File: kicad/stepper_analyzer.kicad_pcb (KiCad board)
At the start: 2 copper layers, 102 x 57 mm, 23 parts, among them J1 Connector_Conn_01x04_Male, J2 Connector_Conn_01x04_Male, M1 Motor, Q1 AO3400A, U1 ACS70331EOLCTR-2P5B3, U2 ACS70331EOLCTR-2P5B3, U3 Pico

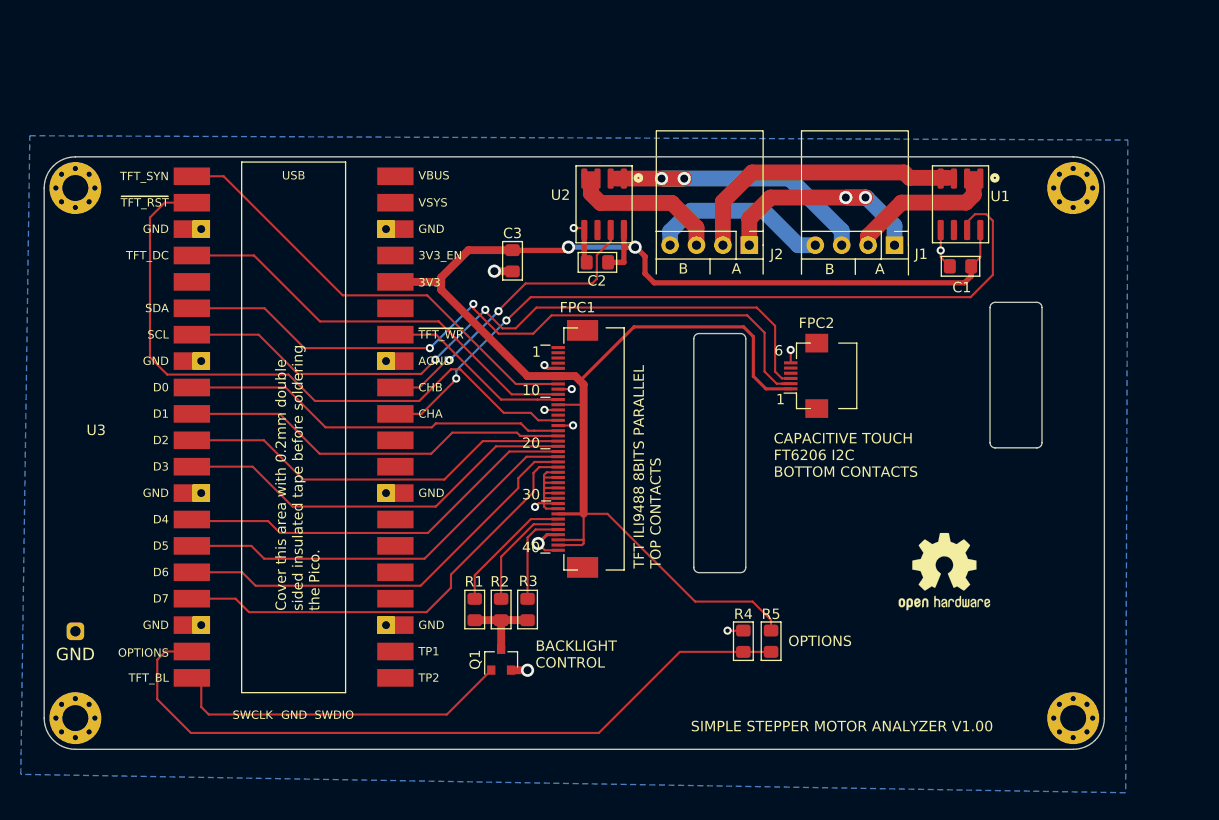
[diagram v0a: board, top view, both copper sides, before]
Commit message: First version, v1.0 of feather
2 stepper motor support using the ACS70311 sensors
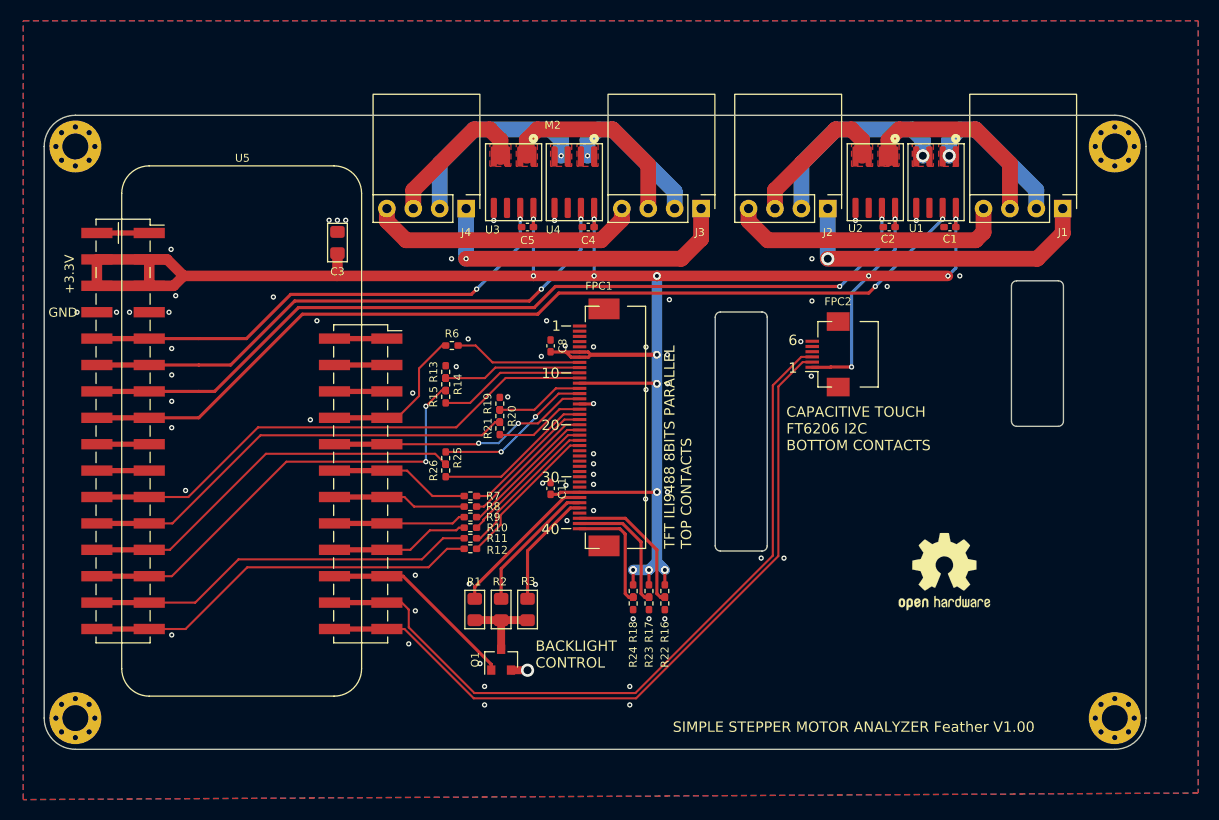
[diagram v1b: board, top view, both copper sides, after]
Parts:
- removed R4, R5: DNP, stepper_motor_analyzer:R_0805_2012Metric_Pad1.15x1.40mm_HandSolder_no_3d
- removed TP3: TestPoint, stepper_motor_analyzer:testpoint_double_side
- added C11: 1u, Capacitor_SMD:C_0402_1005Metric_Pad0.74x0.62mm_HandSolder, F.Cu at (47.7, -25.1)
- added C4: 0.1u, Capacitor_SMD:C_0402_1005Metric_Pad0.74x0.62mm_HandSolder, F.Cu at (51.3, -50.2)
- added C5: 0.1u, Capacitor_SMD:C_0402_1005Metric_Pad0.74x0.62mm_HandSolder, F.Cu at (45.5, -50.2)
- added C8: 1u, Capacitor_SMD:C_0402_1005Metric_Pad0.74x0.62mm_HandSolder, F.Cu at (47.7, -38.8)
- added J3: Connector_Conn_01x04_Male, stepper_motor_analyzer:connector_4pins_horizontal, F.Cu at (62.2, -52.0)
- added J4: Connector_Conn_01x04_Male, stepper_motor_analyzer:connector_4pins_horizontal, F.Cu at (39.6, -52.0)
- added M2: Motor, stepper_motor_analyzer:null_footprint, F.Cu at (36.4, -57.6)
- added R10: 0, Resistor_SMD:R_0402_1005Metric_Pad0.72x0.64mm_HandSolder, F.Cu at (40.0, -21.3)
- added R11: 0, Resistor_SMD:R_0402_1005Metric_Pad0.72x0.64mm_HandSolder, F.Cu at (40.0, -20.3)
- added R12: 0, Resistor_SMD:R_0402_1005Metric_Pad0.72x0.64mm_HandSolder, F.Cu at (40.0, -19.3)
- added R13: 0, Resistor_SMD:R_0402_1005Metric_Pad0.72x0.64mm_HandSolder, F.Cu at (37.6, -36.3)
- added R14: no_stuff, Resistor_SMD:R_0402_1005Metric_Pad0.72x0.64mm_HandSolder, F.Cu at (37.6, -35.1)
- added R15: 0, Resistor_SMD:R_0402_1005Metric_Pad0.72x0.64mm_HandSolder, F.Cu at (37.6, -33.9)
- added R16: 0, Resistor_SMD:R_0402_1005Metric_Pad0.72x0.64mm_HandSolder, F.Cu at (58.7, -15.2)
- added R17: 0, Resistor_SMD:R_0402_1005Metric_Pad0.72x0.64mm_HandSolder, F.Cu at (57.2, -15.2)
- added R18: no_stuff, Resistor_SMD:R_0402_1005Metric_Pad0.72x0.64mm_HandSolder, F.Cu at (55.7, -15.2)
- added R19: 0, Resistor_SMD:R_0402_1005Metric_Pad0.72x0.64mm_HandSolder, F.Cu at (42.8, -33.3)
- added R20: no_stuff, Resistor_SMD:R_0402_1005Metric_Pad0.72x0.64mm_HandSolder, F.Cu at (42.8, -32.1)
- added R21: 0, Resistor_SMD:R_0402_1005Metric_Pad0.72x0.64mm_HandSolder, F.Cu at (42.8, -30.9)
- added R22: no_stuff, Resistor_SMD:R_0402_1005Metric_Pad0.72x0.64mm_HandSolder, F.Cu at (58.7, -14.0)
- added R23: no_stuff, Resistor_SMD:R_0402_1005Metric_Pad0.72x0.64mm_HandSolder, F.Cu at (57.2, -14.0)
- added R24: 0, Resistor_SMD:R_0402_1005Metric_Pad0.72x0.64mm_HandSolder, F.Cu at (55.7, -14.0)
- added R25: no_stuff, Resistor_SMD:R_0402_1005Metric_Pad0.72x0.64mm_HandSolder, F.Cu at (37.6, -28.0)
- added R26: 0, Resistor_SMD:R_0402_1005Metric_Pad0.72x0.64mm_HandSolder, F.Cu at (37.6, -26.8)
- added R6: 0, Resistor_SMD:R_0402_1005Metric_Pad0.72x0.64mm_HandSolder, F.Cu at (38.2, -38.8)
- added R7: 0, Resistor_SMD:R_0402_1005Metric_Pad0.72x0.64mm_HandSolder, F.Cu at (40.0, -24.4)
- added R8: 0, Resistor_SMD:R_0402_1005Metric_Pad0.72x0.64mm_HandSolder, F.Cu at (40.0, -23.4)
- added R9: 0, Resistor_SMD:R_0402_1005Metric_Pad0.72x0.64mm_HandSolder, F.Cu at (40.0, -22.3)
- added U4: ACS70331EOLCTR-2P5B3, stepper_motor_analyzer:SOIC-8_3.9x4.9mm_P1.27mm, F.Cu at (50.0, -54.6)
- added U5: Adafruit_Feather_RP2040, stepper_motor_analyzer:Adafruit_Feather_SMD_2H, F.Cu at (18.0, -30.8)
- C1, C2: footprint stepper_motor_analyzer:C_0805_2012Metric_Pad1.15x1.40mm_HandSolder -> Capacitor_SMD:C_0402_1005Metric_Pad0.74x0.62mm_HandSolder
- U3: value Pico -> ACS70331EOLCTR-2P5B3; footprint stepper_motor_analyzer:Pico_smd_dedicated -> stepper_motor_analyzer:SOIC-8_3.9x4.9mm_P1.27mm
- moved U3 31.7 mm to (44.2, -54.6), turned to -90 degrees
- moved C2 28.3 mm to (80.3, -50.2)
- moved U2 26.2 mm to (79.0, -54.6)
- moved C3 16.9 mm to (27.2, -48.8), turned to -90 degrees
- moved J1 16.6 mm to (97.0, -52.0)
- moved J2 8.33 mm to (74.4, -52.0)
- moved H3 5.66 mm to (102.0, -58.0)
- moved H2 4.00 mm to (2.00, -58.0)
- moved H4 4.00 mm to (102.0, -3.00)
- moved C1 3.91 mm to (86.1, -50.2)
- moved U1 3.17 mm to (84.8, -54.6)
- moved FPC1 2.92 mm to (52.4, -31.0)
- moved FPC2 2.92 mm to (74.7, -38.0)
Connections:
- FPC1 pad 1: Net-(FPC1-Pad1) -> unconnected-(FPC1-Pad1)
- FPC1 pad 11: /~TFT_WR -> /~{TFT_WR}_SCK
- FPC1 pad 13: GND -> /TFT_SDI
- FPC1 pad 14: Net-(FPC1-Pad14) -> /TFT_SDO
- FPC1 pad 15: /~TFT_RST -> /~{TFT_RST}
- FPC1 pad 19: /D2 -> Net-(FPC1-Pad19)
- FPC1 pad 2: Net-(FPC1-Pad2) -> unconnected-(FPC1-Pad2)
- FPC1 pad 20: /D3 -> Net-(FPC1-Pad20)
- FPC1 pad 21: /D4 -> Net-(FPC1-Pad21)
- FPC1 pad 22: /D5 -> Net-(FPC1-Pad22)
- FPC1 pad 23: /D6 -> Net-(FPC1-Pad23)
- FPC1 pad 24: /D7 -> Net-(FPC1-Pad24)
- FPC1 pad 3: Net-(FPC1-Pad3) -> unconnected-(FPC1-Pad3)
- FPC1 pad 38: +3V3 -> /TFT_IM0
- FPC1 pad 39: +3V3 -> /TFT_IM1
- FPC1 pad 4: Net-(FPC1-Pad4) -> unconnected-(FPC1-Pad4)
- FPC1 pad 40: GND -> /TFT_IM2
- FPC1 pad 8: /TFT_SYN -> Net-(FPC1-Pad8)
- FPC1 pad 9: GND -> /~{TFT_CS}
- FPC1 pad MP: (no net) -> GND
- FPC2 pad 4: Net-(FPC2-Pad4) -> unconnected-(FPC2-Pad4)
- FPC2 pad 5: Net-(FPC2-Pad5) -> unconnected-(FPC2-Pad5)
- U1 pad 6: Net-(U1-Pad6) -> unconnected-(U1-Pad6)
- U1 pad 7: /CHA -> /CH1_A
- U2 pad 6: Net-(U2-Pad6) -> unconnected-(U2-Pad6)
- U2 pad 7: /CHB -> /CH1_B
- U3 pad 1: /TFT_SYN -> Net-(J3-Pad3)
- U3 pad 2: /~TFT_RST -> Net-(J3-Pad3)
- U3 pad 3: GND -> Net-(J4-Pad3)
- U3 pad 4: /TFT_DC -> Net-(J4-Pad3)
- U3 pad 5: Net-(U3-Pad5) -> GND
- U3 pad 6: /SDA -> unconnected-(U3-Pad6)
- U3 pad 7: /SCL -> /CH2_B
- U3 pad 8: GND -> +3V3
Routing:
- net /CH1_A: track 0.00 -> 90.4 mm, vias 0 -> 2
- net /CH1_B: track 0.00 -> 84.9 mm, vias 0 -> 2
- net /CHA: track 73.4 -> 0.00 mm, vias 2 -> 0
- net /OPTIONS: track 72.0 -> 0.00 mm
- net /~TFT_RST: track 63.3 -> 0.00 mm
- net /CH2_A: track 0.00 -> 55.2 mm, vias 0 -> 2
- net /~{TFT_WR}_SCK: track 0.00 -> 51.2 mm
- net /CH2_B: track 0.00 -> 48.1 mm, vias 0 -> 2
- net +3V3: track 165.2 -> 211.2 mm, vias 2 -> 16
- net /TFT_DC_CS: track 0.00 -> 44.1 mm, vias 0 -> 2
- net /TFT_D0_SDI: track 0.00 -> 42.8 mm
- net /TFT_D1_SDO: track 0.00 -> 37.8 mm
- net GND: track 39.3 -> 2.93 mm, vias 12 -> 69
- net Net-(J3-Pad1): track 0.00 -> 31.1 mm, vias 0 -> 1
- net /CHB: track 29.9 -> 0.00 mm, vias 2 -> 0
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- added copper zone on F.Cu, net GND
- added copper zone on F.Cu, net Net-(J1-Pad2)
- added copper zone on F.Cu, net Net-(J1-Pad3)
- added copper zone on F.Cu, net Net-(J2-Pad2)
- added copper zone on F.Cu, net Net-(J2-Pad3)
- added copper zone on F.Cu, net Net-(J3-Pad2)
- added copper zone on F.Cu, net Net-(J3-Pad3)
- added copper zone on F.Cu, net Net-(J4-Pad2)
- added copper zone on F.Cu, net Net-(J4-Pad3)
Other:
- board size 102 x 57 mm -> 106 x 61 mm
- net class Default removed
- board text added: "+3.3V"
- board text added: "SIMPLE STEPPER MOTOR ANALYZER Feather V1.00"
- board text removed: "A"
- board text removed: "B"
- board text removed: "Cover this area with 0.2mm double sided insulated tape before soldering the Pico."
- board text removed: "OPTIONS"
- board text removed: "SIMPLE STEPPER MOTOR ANALYZER V1.00"

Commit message: Update PCB to use TMCS1100A4QDRQ1
TMCS1100A4QDRQ1 is compatible with the old current sense device, except needs a reference voltage.
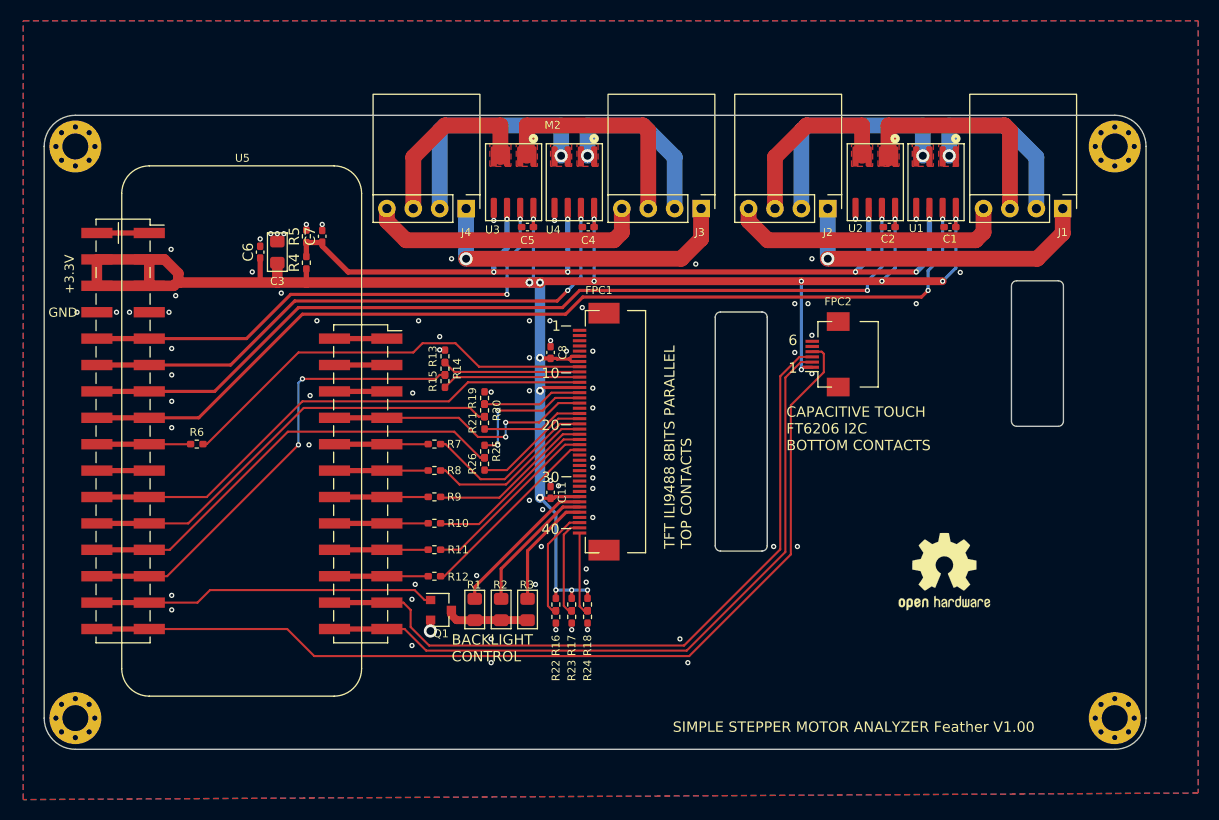
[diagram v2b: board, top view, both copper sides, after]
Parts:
- added C6: 1u, Capacitor_SMD:C_0402_1005Metric_Pad0.74x0.62mm_HandSolder, F.Cu at (19.8, -47.8)
- added C7: 1u, Capacitor_SMD:C_0402_1005Metric_Pad0.74x0.62mm_HandSolder, F.Cu at (25.7, -49.4)
- added R4: 4.7k, Resistor_SMD:R_0402_1005Metric_Pad0.72x0.64mm_HandSolder, F.Cu at (24.2, -46.8)
- added R5: 4.7k, Resistor_SMD:R_0402_1005Metric_Pad0.72x0.64mm_HandSolder, F.Cu at (24.2, -49.4)
- U1, U2, U3, U4: value ACS70331EOLCTR-2P5B3 -> TMCS1100A4QDRQ1
- moved R6 26.3 mm to (13.7, -29.4)
- moved R16 10.6 mm to (48.2, -13.9)
- moved R22 10.6 mm to (48.2, -12.7)
- moved R17 7.55 mm to (49.8, -13.9)
- moved R23 7.55 mm to (49.8, -12.7)
- moved Q1 7.51 mm to (37.2, -13.4), turned to 0 degrees
- moved R7 6.08 mm to (36.5, -29.4)
- moved C3 5.86 mm to (21.4, -47.8)
- moved R8 4.90 mm to (36.5, -26.8)
- moved R18 4.57 mm to (51.3, -13.9)
- moved R24 4.57 mm to (51.3, -12.7)
- moved R12 4.35 mm to (36.5, -16.6)
- moved R9 3.97 mm to (36.5, -24.3)
- moved R25 3.79 mm to (41.4, -28.7)
- moved R26 3.79 mm to (41.4, -27.5)
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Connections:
- FPC2 pad 4: unconnected-(FPC2-Pad4) -> /TP_INT
- U1 pad 6: unconnected-(U1-Pad6) -> /VREF
- U2 pad 6: unconnected-(U2-Pad6) -> /VREF
- U3 pad 6: unconnected-(U3-Pad6) -> /VREF
- U4 pad 6: unconnected-(U4-Pad6) -> /VREF
- U5 pad 15: /D6 -> /TFT_BL
- U5 pad 16: /D7 -> /TP_INT
- U5 pad 19: /TFT_BL -> /D7
- U5 pad 20: /D5 -> /D6
- U5 pad 21: /D4 -> /D5
- U5 pad 22: /D3 -> /D4
- U5 pad 23: /D2 -> /D3
- U5 pad 24: /~{TFT_RST} -> /D2
- U5 pad 25: /TFT_SYN -> /~{TFT_RST}
- U5 pad 9: unconnected-(U5-Pad9) -> /TFT_SYN
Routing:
- net /TP_INT: track 0.00 -> 93.7 mm
- net /VREF: track 0.00 -> 87.7 mm, vias 0 -> 8
- net /D7: track 38.5 -> 9.02 mm
- net /D6: track 37.9 -> 9.02 mm
- net Net-(FPC1-Pad8): track 12.4 -> 41.2 mm
- net +3V3: track 211.2 -> 193.1 mm, vias 16 -> 17
- net /TFT_BL: track 19.1 -> 33.0 mm
- net /TFT_SYN: track 15.1 -> 9.02 mm
- net /TFT_D1_SDO: track 37.8 -> 43.0 mm
- net unconnected-(U5-Pad9): track 5.04 -> 0.00 mm
- net /D2: track 13.5 -> 9.02 mm
- net /D5: track 13.4 -> 9.02 mm
- net /D1: track 15.4 -> 11.2 mm
- net Net-(FPC1-Pad19): track 13.0 -> 17.0 mm
- net /D3: track 12.9 -> 9.02 mm
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
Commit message: minor changes
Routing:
- net /TP_INT: track 93.7 -> 94.6 mm
- net GND: vias 79 -> 83
